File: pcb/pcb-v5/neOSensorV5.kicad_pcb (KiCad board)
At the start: 2 copper layers, 54 parts, among them J1 Conn_01x04, J2 Conn_01x04, J3 Conn_01x05, J4 Conn_01x05, J5 Conn_01x05, J6 Conn_01x03, J7 Conn_01x03, J8 Conn_01x03, J9 Conn_01x03, Q1 2N7002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

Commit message: update PCB v5
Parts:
- added REF**: OSHW-Logo_7.5x8mm_SilkScreen, Symbol:OSHW-Logo_7.5x8mm_SilkScreen, B.Cu at (64.0, 70.4)
- SW1, SW2, SW3, U5: moved to B.Cu
- moved J6 216.7 mm to (31.2, 44.5)
- moved U1 186.1 mm to (49.5, 52.3)
- moved J4 181.7 mm to (46.7, 73.2), turned to 90 degrees
- moved C2 171.1 mm to (39.9, 69.3), turned to 270 degrees
- moved H2 169.9 mm to (71.6, 71.6)
- moved C1 169.3 mm to (43.2, 111.8)
- moved R1 169.3 mm to (47.9, 111.8)
- moved R4 169.3 mm to (57.4, 112.2)
- moved R9 169.3 mm to (38.4, 111.8)
- moved C3 169.3 mm to (88.6, 96.2)
- moved C4 169.3 mm to (100.8, 85.3)
- moved C5 169.3 mm to (112.2, 72.5)
- moved Q1 169.3 mm to (102.2, 89.1)
- moved R10 169.3 mm to (88.6, 93.3)
- moved R11 169.3 mm to (83.8, 95.0)
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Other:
- board outline added: 49.5 x 49.5 mm
- board text added: "(c)neO"
- board text added: "+"
- board text added: "-"
- board text added: "CLR/OK"
- board text added: "Campus"
- board text added: "neOSensor v5"

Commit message: update pcb V5
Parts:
- removed J7, J8, J9: Conn_01x03, Connector_PinHeader_2.54mm:PinHeader_1x03_P2.54mm_Vertical
- removed REF**: OSHW-Logo_7.5x8mm_SilkScreen, Symbol:OSHW-Logo_7.5x8mm_SilkScreen
- J6: value Conn_01x03 -> Conn_01x06; footprint Connector_PinHeader_2.54mm:PinHeader_1x03_P2.54mm_Vertical -> Connector_PinHeader_2.54mm:PinHeader_1x06_P2.54mm_Vertical
- moved J3 46.2 mm to (27.2, 51.6)
- moved J5 43.2 mm to (70.1, 47.0)
- moved C1 36.6 mm to (15.0, 88.4)
- moved R1 36.6 mm to (19.7, 88.4)
- moved R4 36.6 mm to (29.2, 88.8)
- moved R9 36.6 mm to (10.2, 88.4)
- moved R16 36.6 mm to (46.9, 84.6)
- moved R18 36.6 mm to (43.7, 88.0)
- moved R6 36.6 mm to (39.0, 88.0)
- moved R19 36.6 mm to (51.7, 81.7)
- moved R3 36.6 mm to (24.5, 89.7)
- moved R8 36.6 mm to (46.9, 81.7)
- moved TP5 36.6 mm to (51.6, 85.5)
- moved TP4 21.9 mm to (90.6, 72.7)
- moved C5 21.9 mm to (90.6, 68.9)
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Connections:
- J6 pad 2: /ANA_0 -> GND
- J6 pad 3: GND -> /ANA_0
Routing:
- net +5V: track 0.00 -> 6.84 mm, vias 0 -> 1
- net +3V3: track 0.00 -> 6.30 mm, vias 0 -> 6
- added copper zone on B.Cu, net +3V3
- added copper zone on F.Cu, net +3V3
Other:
- board text added: "M2SIAME FEB21 FE/FE/FT"

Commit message: update PCB v5
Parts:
- moved D1 33.0 mm to (35.0, 27.4)
- moved C1 29.5 mm to (33.0, 65.0), turned to 180 degrees
- moved SW1 4.83 mm to (64.5, 25.5)
- moved SW2 4.83 mm to (43.6, 25.5)
- moved SW3 4.83 mm to (54.0, 25.5)
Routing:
- net +5V: track 6.84 -> 68.6 mm, vias 1 -> 4
- net GND: vias 0 -> 16
- net +3V3: vias 6 -> 10

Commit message: update PCB v5
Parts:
- removed TP1: tp_tx2, TestPoint:TestPoint_Loop_D2.50mm_Drill1.0mm
- removed TP2: tp_rx2, TestPoint:TestPoint_Loop_D2.50mm_Drill1.0mm
- removed TP7: tp_INT, TestPoint:TestPoint_Loop_D2.50mm_Drill1.0mm
- C5, Q1, R1, R13, R14, R15, R18, R2, R4, R5, R6, R7: moved to B.Cu
- moved Q1 79.1 mm to (36.3, 31.8), turned to 90 degrees
- moved R4 69.8 mm to (70.2, 32.3), turned to 180 degrees
- moved R17 64.4 mm to (34.7, 48.3)
- moved R9 64.1 mm to (48.8, 37.2), turned to 180 degrees
- moved R13 62.2 mm to (34.7, 48.3)
- moved C4 60.7 mm to (58.8, 33.0)
- moved R3 60.3 mm to (41.3, 31.9), turned to 90 degrees
- moved R2 59.3 mm to (40.3, 30.9)
- moved R7 57.2 mm to (57.8, 32.0), turned to 270 degrees
- moved R20 56.7 mm to (34.7, 46.5)
- moved R1 56.3 mm to (33.3, 33.8), turned to 270 degrees
- moved R10 55.5 mm to (58.8, 31.0), turned to 180 degrees
- moved R14 54.4 mm to (34.7, 46.5)
- moved TP6 54.1 mm to (52.3, 48.8)
- moved R11 53.4 mm to (65.9, 33.0)
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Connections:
- D1 pad 2: +5V -> Net-(D1-Pad2)
- Q1 pad 2: Net-(Q1-Pad2) -> Net-(D1-Pad1)
- R1 pad 1: Net-(Q1-Pad2) -> Net-(D1-Pad2)
- R1 pad 2: Net-(D1-Pad1) -> +5V
- SW1 pad 1: Net-(Q1-Pad1) -> +3V3
- SW1 pad 2: +3V3 -> Net-(Q1-Pad1)
- SW2 pad 1: +3V3 -> Net-(R10-Pad2)
- SW2 pad 2: Net-(R10-Pad2) -> +3V3
- SW3 pad 1: +3V3 -> Net-(R11-Pad1)
- SW3 pad 2: Net-(R11-Pad1) -> +3V3
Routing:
- net +3V3: track 6.30 -> 186.9 mm, vias 10 -> 23
- net /SCL: track 0.00 -> 136.4 mm, vias 0 -> 7
- net /SDA: track 0.00 -> 124.3 mm, vias 0 -> 4
- net /INT: track 0.00 -> 69.8 mm, vias 0 -> 1
- net /PM_EN: track 0.00 -> 36.1 mm, vias 0 -> 3
- net Net-(R6-Pad2): track 0.00 -> 29.2 mm, vias 0 -> 3
- net Net-(R5-Pad2): track 0.00 -> 24.1 mm, vias 0 -> 3
- net /LED: track 0.00 -> 19.9 mm, vias 0 -> 3
- net +5V: track 68.6 -> 83.4 mm, vias 4 -> 5
- net /SW3: track 0.00 -> 11.1 mm, vias 0 -> 2
- net Net-(Q1-Pad1): track 0.00 -> 7.55 mm, vias 0 -> 2
- net /SW2: track 0.00 -> 6.65 mm, vias 0 -> 1
- net /IR: track 0.00 -> 6.46 mm
- net Net-(R11-Pad1): track 0.00 -> 5.62 mm, vias 0 -> 1
- net Net-(R10-Pad2): track 0.00 -> 3.11 mm, vias 0 -> 2
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
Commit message: update
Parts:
- added REF**: OSHW-Logo_7.5x8mm_SilkScreen, Symbol:OSHW-Logo_7.5x8mm_SilkScreen, F.Cu at (62.4, 70.4)
- moved TP3 9.16 mm to (56.5, 53.8)
- moved TP4 5.30 mm to (53.3, 51.8)
- moved TP6 1.83 mm to (53.3, 47.2)
- moved U4 0.46 mm to (31.1, 70.2)
- moved TP5 0.46 mm to (56.6, 49.0)
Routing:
- net /ADC1_3: track 0.00 -> 45.0 mm, vias 0 -> 5
- net /ADC1_6: track 0.00 -> 41.3 mm, vias 0 -> 1
- net /ADC1_0: track 0.00 -> 36.3 mm, vias 0 -> 2
- net /ADC1_7: track 0.00 -> 33.9 mm, vias 0 -> 1
- net Net-(R14-Pad2): track 0.00 -> 12.3 mm, vias 0 -> 1
- net Net-(R15-Pad2): track 0.00 -> 11.7 mm, vias 0 -> 1
- net Net-(R13-Pad2): track 0.00 -> 10.3 mm, vias 0 -> 1
- net Net-(R18-Pad2): track 0.00 -> 10.2 mm, vias 0 -> 3
- net /ANA_3: track 0.00 -> 2.96 mm
- net /ANA_1: track 0.00 -> 2.74 mm
- net /ANA_2: track 0.00 -> 2.64 mm
- net /ANA_0: track 0.00 -> 2.43 mm
- net +3V3: track 186.9 -> 189.1 mm, vias 23 -> 25
- net GND: vias 16 -> 29
- added copper zone on B.Cu, net GND
- added copper zone on F.Cu, net GND
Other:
- board text added: "Sensor v5"
- board text added: "neO"
- board text removed: "neOSensor v5"

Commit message: update PCB v5
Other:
- board text added: "M2SIAME FEB21 FE/FT"
- board text removed: "M2SIAME FEB21 FE/FE/FT"

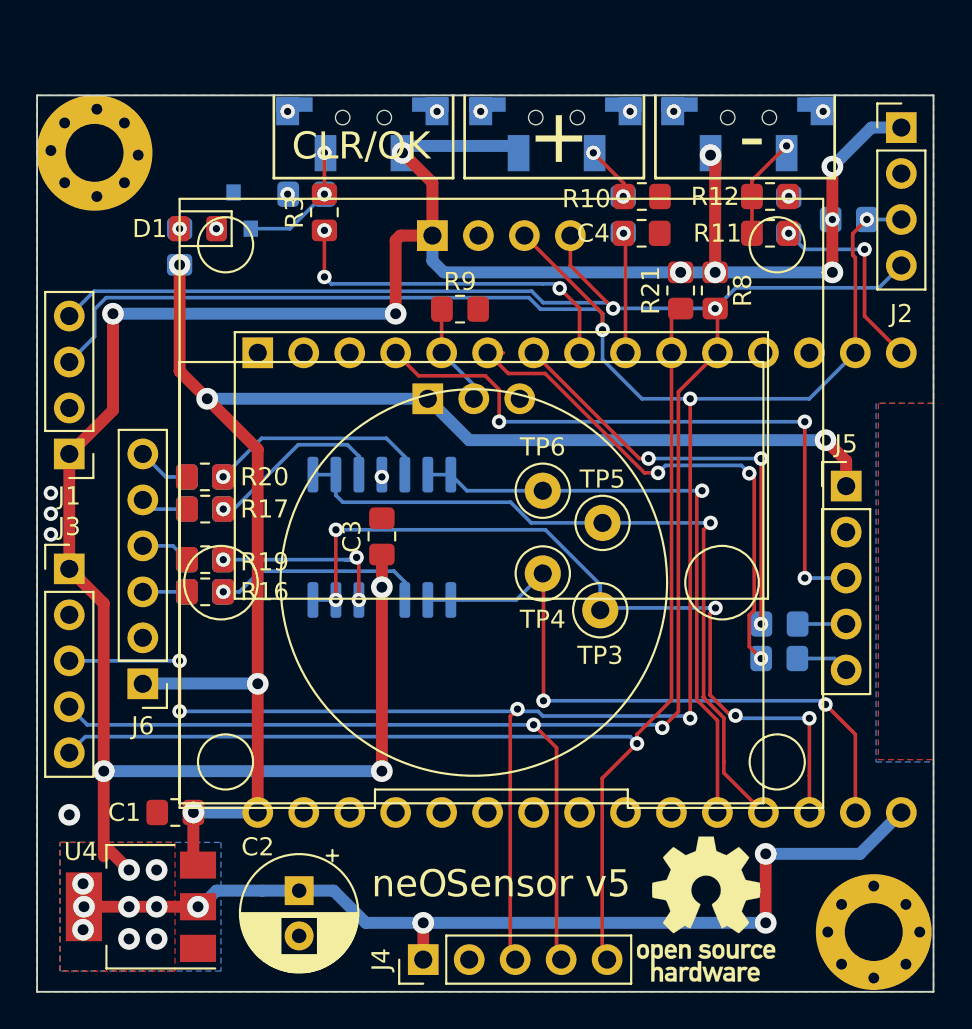
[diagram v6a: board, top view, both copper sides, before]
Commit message: added nodes labels and minor corrections to pcb v5
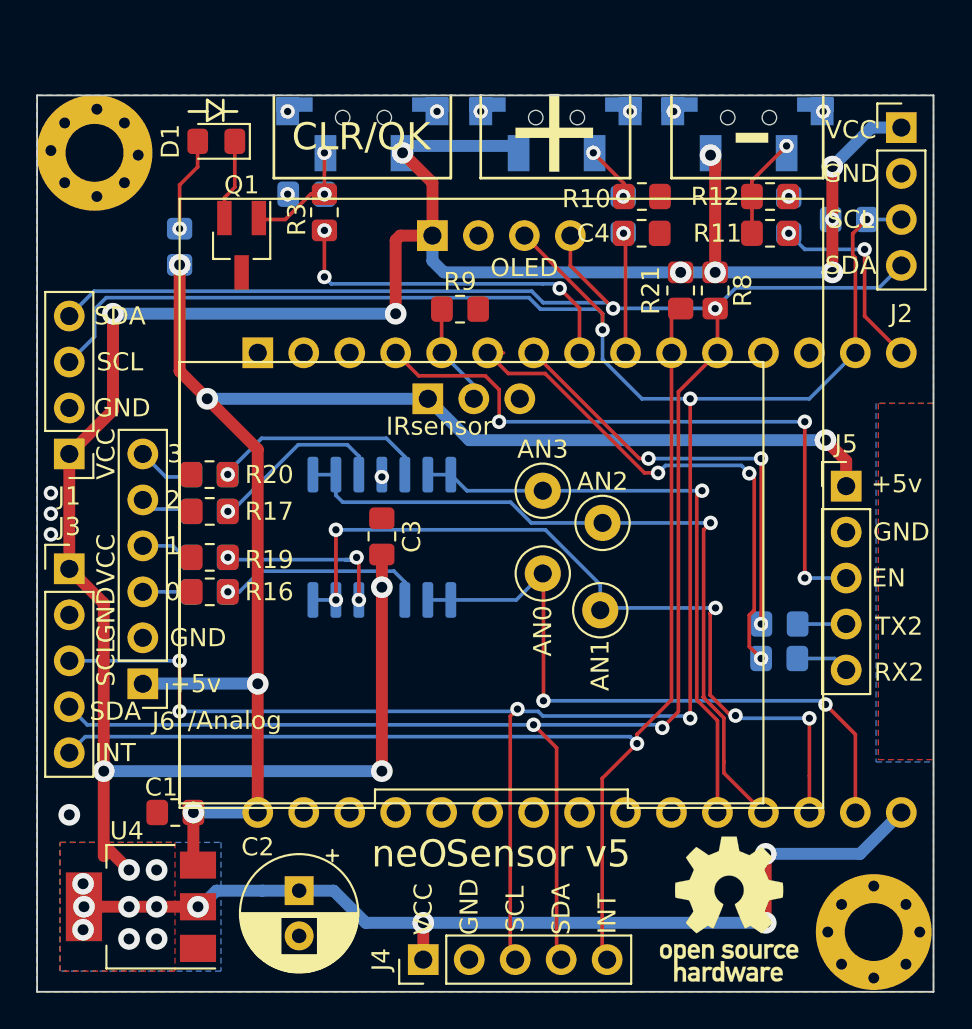
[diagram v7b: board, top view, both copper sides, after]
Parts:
- Q1: footprint Package_TO_SOT_SMD:SOT-23 -> Package_TO_SOT_SMD:SOT-23_Handsoldering; moved to F.Cu
- moved D1 4.93 mm to (35.3, 27.9)
- moved Q1 1.96 mm to (36.7, 33.7), turned to 270 degrees
- moved REF** 1.27 mm to (63.6, 70.4)
- moved R17 0.28 mm to (34.9, 48.4)
- moved R19 0.28 mm to (34.9, 50.9)
- moved R13 0.28 mm to (34.9, 48.4)
- moved R14 0.28 mm to (34.9, 46.4)
- moved R18 0.28 mm to (34.9, 50.9)
- moved R20 0.28 mm to (34.9, 46.4)
- moved R16 0.25 mm to (34.9, 52.8)
- moved R15 0.25 mm to (34.9, 52.8)
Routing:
- net Net-(D1-Pad2): track 0.00 -> 5.24 mm
- net Net-(D1-Pad1): track 0.00 -> 4.47 mm, vias 1 -> 0
- net Net-(Q1-Pad1): track 7.55 -> 6.92 mm
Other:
- board text added: "+5v"
- board text added: "/Analog"
- board text added: "0"
- board text added: "1"
- board text added: "2"
- board text added: "3"
- board text added: "AN0"
- board text added: "AN1"
- board text added: "AN2"
- board text added: "AN3"
- board text added: "EN"
- board text added: "ESP32"
- board text added: "GND"
- board text added: "INT"
- board text added: "IRsensor"
- board text added: "OLED"
- board text added: "RX2"
- board text added: "SCL"
- board text added: "SDA"
- board text added: "TX2"
- board text added: "Univ.Tlse3/IRIT"
- board text added: "VCC"
